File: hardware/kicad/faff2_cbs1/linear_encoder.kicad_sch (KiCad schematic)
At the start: 24 parts, among them J601 FH12-10S-0.5SH(55), J602 FTSH-105-01-L-DV-K-TR, J603 8510-4500PL, U601 AM26LV32

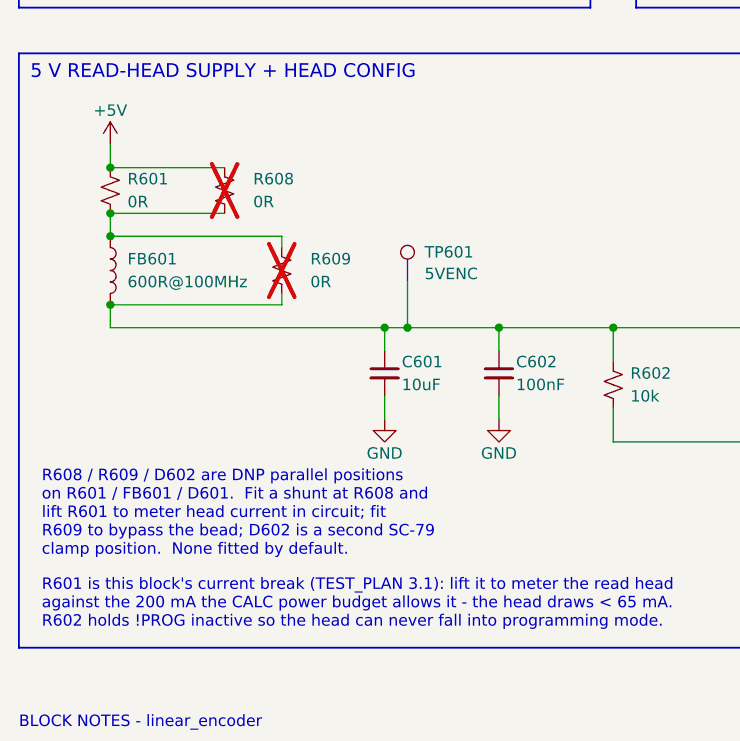
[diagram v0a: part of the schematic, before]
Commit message: review r4 items 7,8,13 and the PWR1131 ruling: parts, not placement
Items 7 and 8, R608 and R609 go. Review round R6 asked for DNP parallel
positions across R601, FB601 and D601; the captain has reversed two of the
three, and the reasoning is better than the original: R608 and R601 are the same
0603, so to meter head current you replace R601 with a shunt rather than
populate a second footprint beside it, and FB601 can be lifted and bridged
instead of fitting R609. D602 stays - a second clamp POSITION, for a different
clamp voltage or a bidirectional part, is not the same argument. Both the sheet
note and actuator-rev-afe.md's R6 row now carry the reversal rather than
quietly dropping it.

Item 13, R1128..R1133 were the only 100R in the design on a project-local
symbol: faff2_passives:RES_TF_100R_0603_H, a pre-rotated variant round 2 added
so they could lie horizontally without instance rotation - that was the reason,
and it does not outweigh nine other 100R across mcu, ui_io and motor_drive using
the house Amodo_Resistors:RES_TF_100R_0603. They unify onto it, rotated 90 with
field angles compensated to 270, which AGENTS.md permits on exactly that
condition and which a render confirms: horizontal body, horizontal text. The
local variant now has no users and is deleted from both the sheet and
faff2_passives, and AGENTS.md's guidance flips to prefer the house symbol.

The captain's third round-3 answer: R1120 and its +3V3 flag drag 7.62 mm down
into the clear space below, same connectivity, and the gate-drive bus no longer
crosses the arrow. No bus reroute, as instructed. Dropping it put R1120's
reference 0.02 mm off R1117's body, so the reference centres in the 6.85 mm
between the two.

The design is now clean under tools/check_text_clearance.py --margin 0.35 for
the first time - zero findings on all ten sheets.

ERC 0/0 at severity-all; 406 components, 264 nets. The only netlist change is
the two removals.

Co-Authored-By: Claude Opus 5 <noreply@anthropic.com>
Claude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
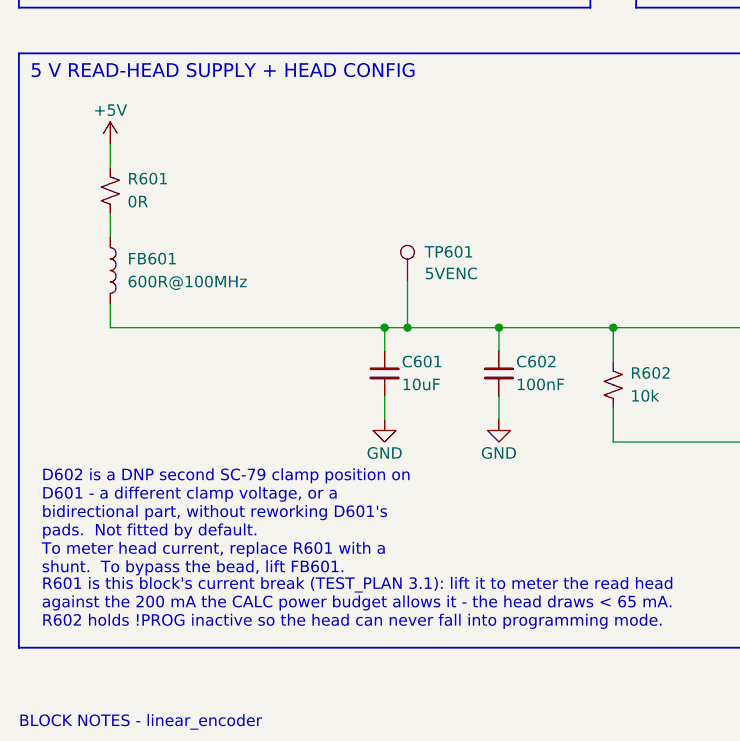
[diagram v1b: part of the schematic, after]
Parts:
- removed R608, R609: 0R, Amodo:R_0603_1608Metric, symbol Amodo_Resistors:RES_TF_0R_0603
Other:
- note added: "D602 is a DNP second SC-79 clamp position on D601 - a different clamp voltage, or a bidirectional part, without reworking D601's pads. Not fitted by default. To meter head current, replace R601 with a shunt. To bypass the bead, lift FB601."
- note removed: "R608 / R609 / D602 are DNP parallel positions on R601 / FB601 / D601. Fit a shunt at R608 and lift R601 to meter head current in circuit; fit R609 to bypass the bead; D602 is a second SC-79 clamp position. None fitted by default."
